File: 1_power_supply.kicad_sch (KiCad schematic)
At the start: 38 parts

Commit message: feat: power supply updates and mcu kickoff
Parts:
- added C?: 100u, symbol Device:C_Polarized_Small
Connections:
- net +BATT: now also C?.1
- net GND: now also C?.2
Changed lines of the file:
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@@
   (junction (at 190.5 64.77) (diameter 0) (color 0 0 0 0)
   )
+  (junction (at 238.125 61.595) (diameter 0) (color 0 0 0 0)
+  )
   (junction (at 217.805 61.595) (diameter 0) (color 0 0 0 0)
   )
@@
   (junction (at 29.845 66.04) (diameter 0) (color 0 0 0 0)
   )
+  (junction (at 238.125 50.165) (diameter 0) (color 0 0 0 0)
+  )
   (junction (at 39.37 111.76) (diameter 0) (color 0 0 0 0)
   )
@@
     (stroke (width 0) (type default) (color 0 0 0 0))
   )
-  (polyline (pts (xy 249.555 36.83) (xy 209.55 36.83))
+  (polyline (pts (xy 259.715 36.83) (xy 209.55 36.83))
     (stroke (width 0) (type default) (color 0 0 0 0))
   )
@@
     (stroke (width 0) (type default) (color 0 0 0 0))
   )
-  (polyline (pts (xy 209.55 80.01) (xy 249.555 80.01))
+  (polyline (pts (xy 209.55 80.01) (xy 259.715 80.01))
     (stroke (width 0) (type default) (color 0 0 0 0))
   )
@@
     (stroke (width 0) (type default) (color 0 0 0 0))
   )
+  (wire (pts (xy 248.285 53.34) (xy 248.285 50.165))
+    (stroke (width 0) (type default) (color 0 0 0 0))
+  )
   (wire (pts (xy 91.44 111.76) (xy 93.98 111.76))
     (stroke (width 0) (type default) (color 0 0 0 0))
@@
     (stroke (width 0) (type default) (color 0 0 0 0))
   )
+  (wire (pts (xy 248.285 61.595) (xy 238.125 61.595))
+    (stroke (width 0) (type default) (color 0 0 0 0))
+  )
   (wire (pts (xy 66.04 53.975) (xy 66.04 62.23))
     (stroke (width 0) (type default) (color 0 0 0 0))
@@
     (stroke (width 0) (type default) (color 0 0 0 0))
   )
-  (polyline (pts (xy 249.555 80.01) (xy 249.555 36.83))
+  (polyline (pts (xy 259.715 80.01) (xy 259.715 36.83))
     (stroke (width 0) (type default) (color 0 0 0 0))
   )
@@
     (stroke (width 0) (type default) (color 0 0 0 0))
   )
+  (wire (pts (xy 248.285 58.42) (xy 248.285 61.595))
+    (stroke (width 0) (type default) (color 0 0 0 0))
+  )
   (wire (pts (xy 81.915 78.105) (xy 81.915 80.01))
     (stroke (width 0) (type default) (color 0 0 0 0))
@@
   )
   (wire (pts (xy 101.6 111.76) (xy 106.045 111.76))
+    (stroke (width 0) (type default) (color 0 0 0 0))
+  )
+  (wire (pts (xy 248.285 50.165) (xy 238.125 50.165))
     (stroke (width 0) (type default) (color 0 0 0 0))
   )
@@
       (effects (font (size 1.27 1.27)) hide)
     )
+    (pin "1")
+    (pin "2")
+  )
+  (symbol (lib_id "Device:C_Polarized_Small") (at 248.285 55.88 0) (unit 1)
+    (in_bom yes) (on_board yes)
+    (property "Reference" "C?" (id 0) (at 250.825 54.61 0)
+      (effects (font (size 1.27 1.27)) (justify left))
+    )
+    (property "Value" "100u" (id 1) (at 250.825 57.15 0)
+      (effects (font (size 1.27 1.27)) (justify left))
+    )
+    (property "Footprint" "" (id 2) (at 248.285 55.88 0)
+      (effects (font (size 1.27 1.27)) hide)
+    )
+    (property "Datasheet" "~" (id 3) (at 248.285 55.88 0)
+      (effects (font (size 1.27 1.27)) hide)
+    )

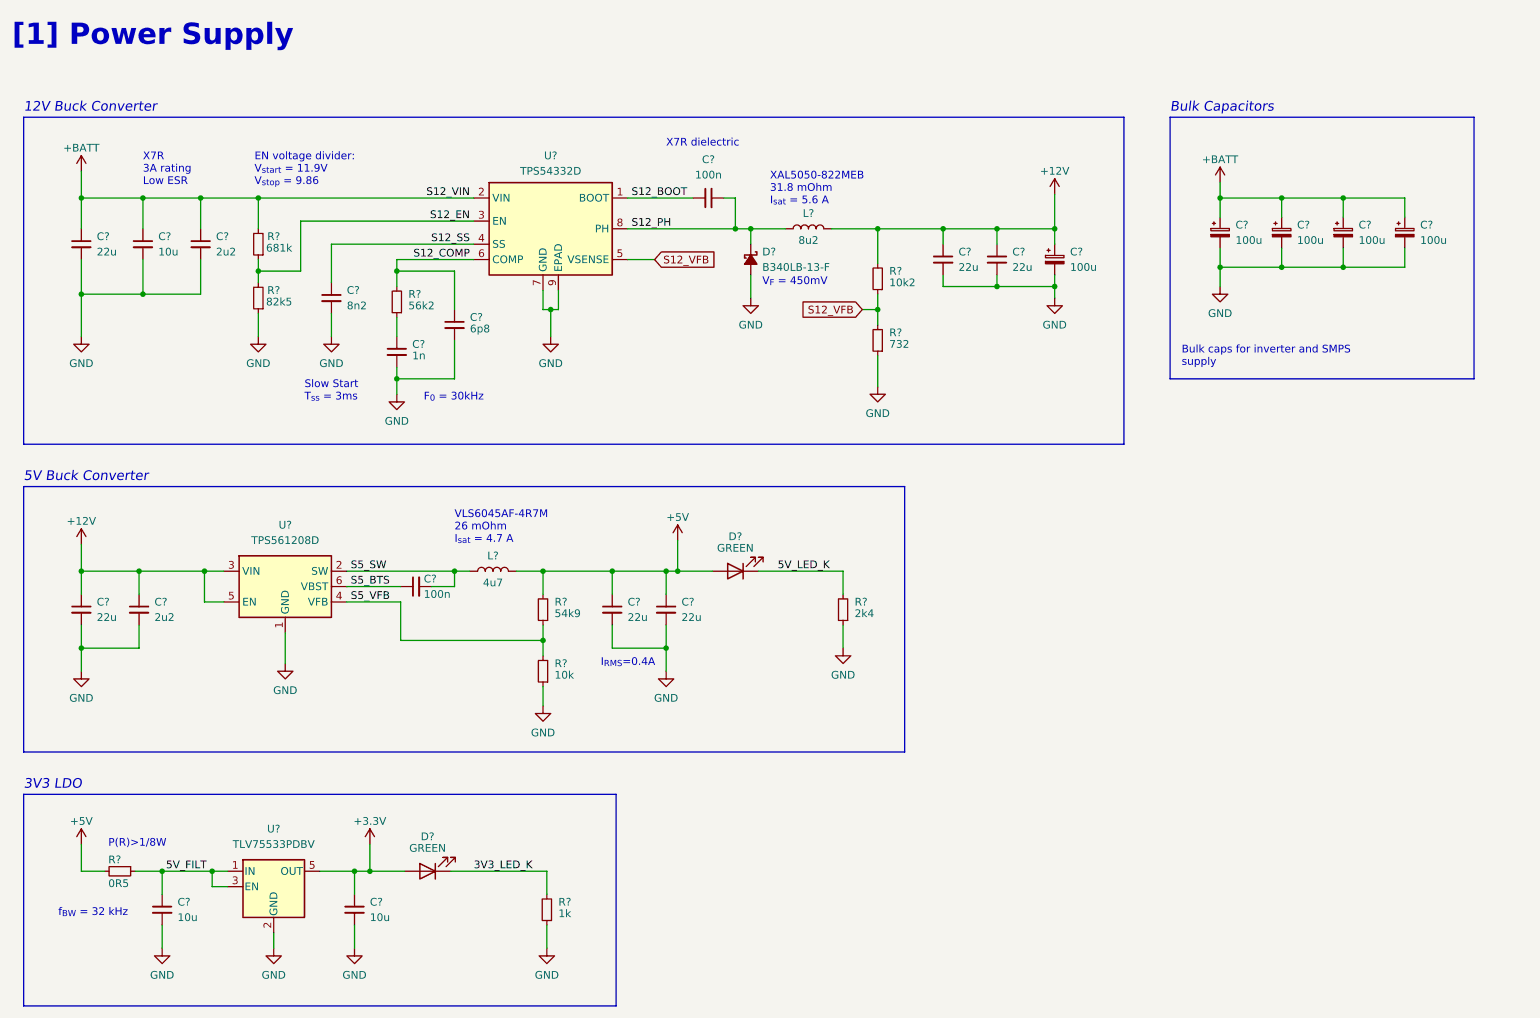
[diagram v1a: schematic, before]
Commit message: feat/chore: MCU supply caps and filter circuitry and updated component references in power supply sheet
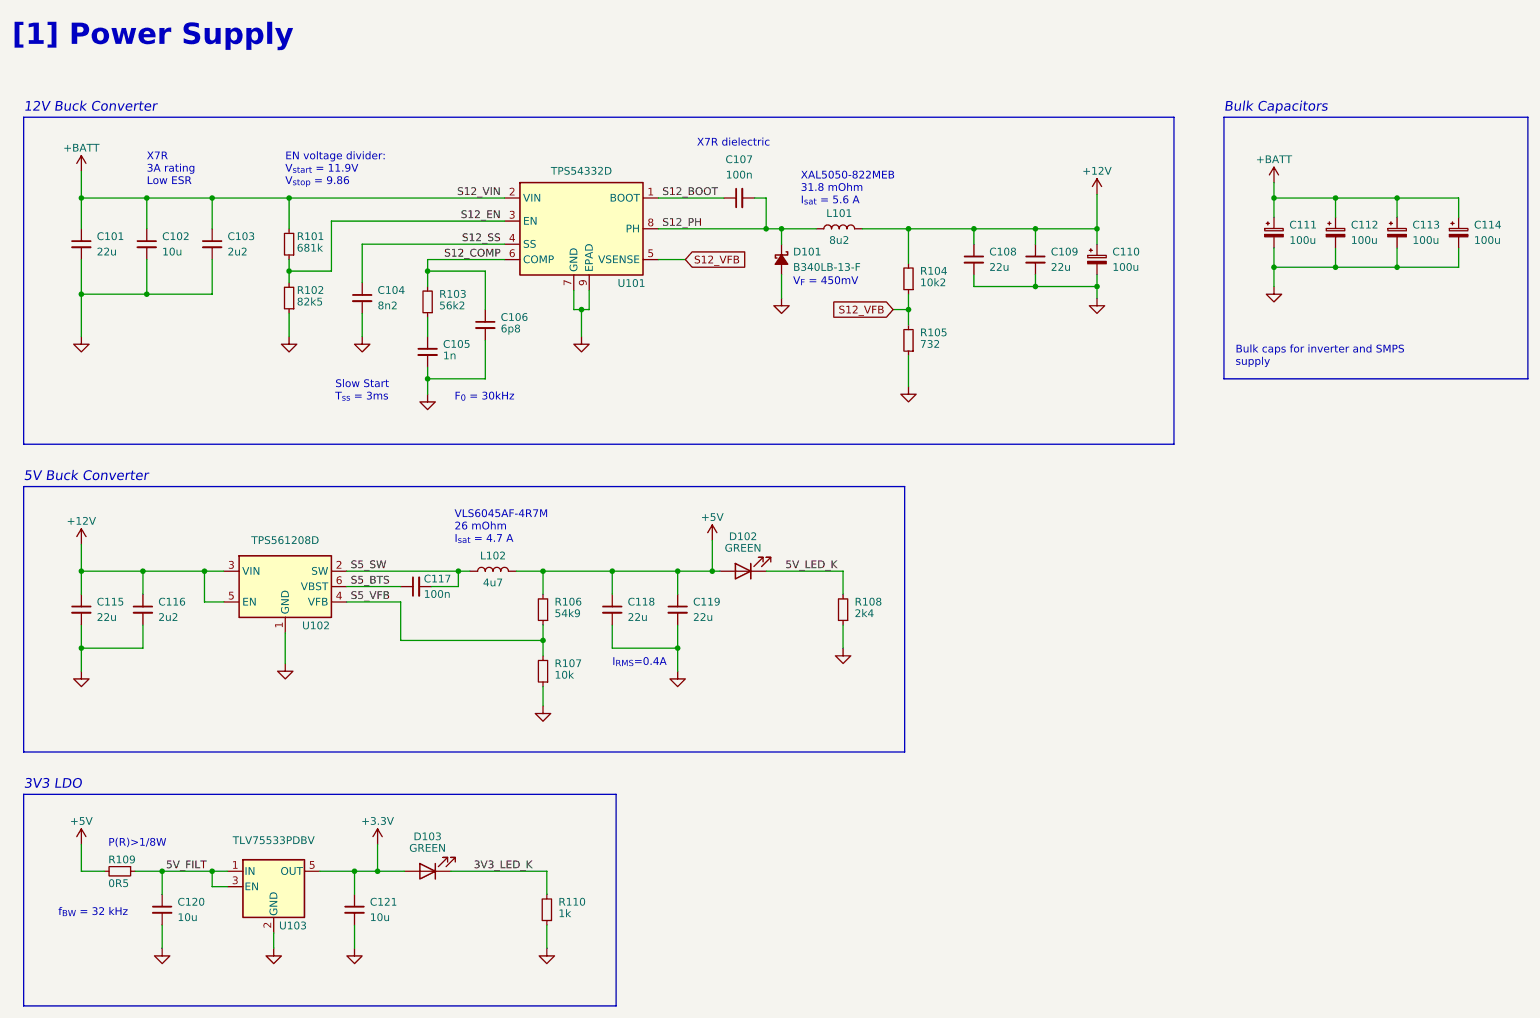
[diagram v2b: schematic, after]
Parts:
- gave numbers to parts that had none: 39
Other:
- moved on the sheet: C102, C103, C104, C105, C106, C107, C108, C109, C110, C111, C112, C113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

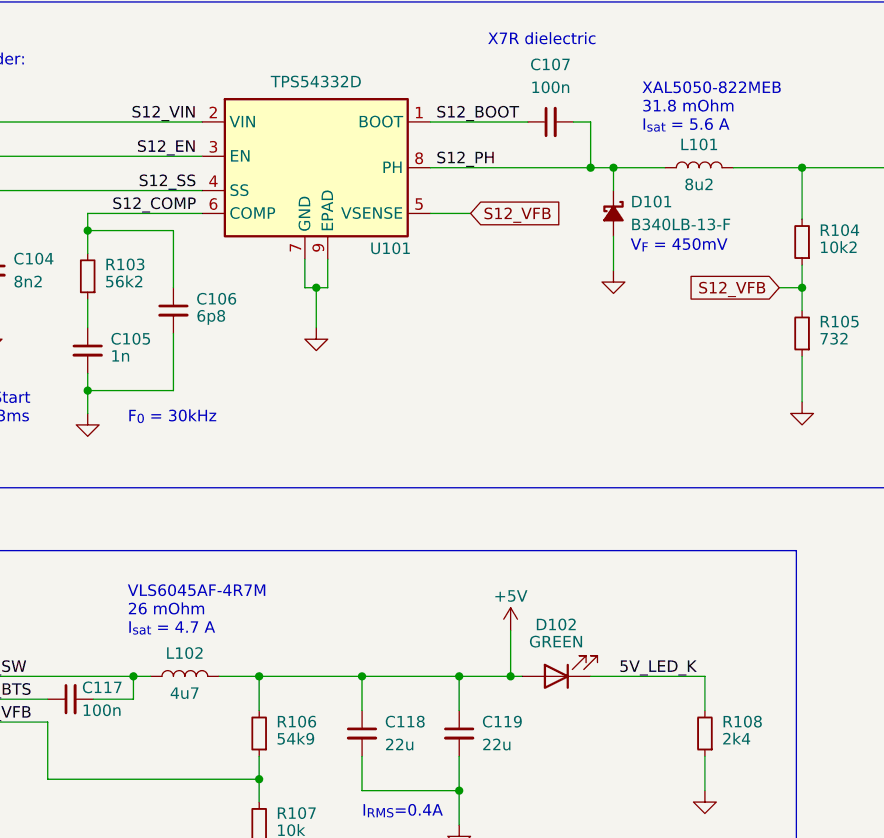
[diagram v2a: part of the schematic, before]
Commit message: feat: initial peripheral circuitry for MCU
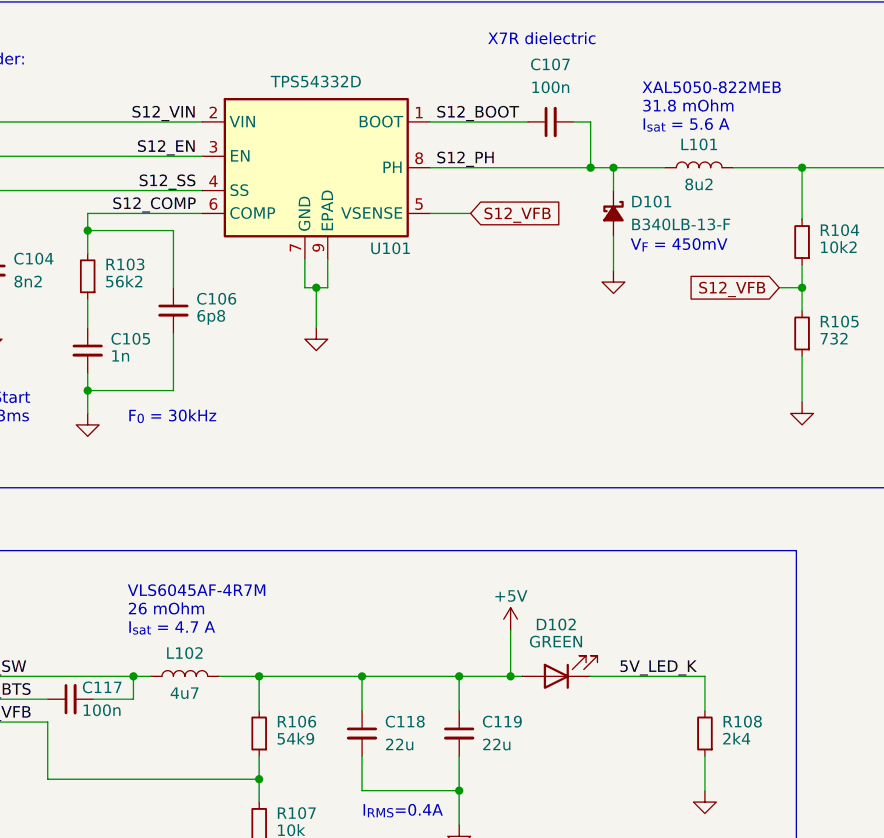
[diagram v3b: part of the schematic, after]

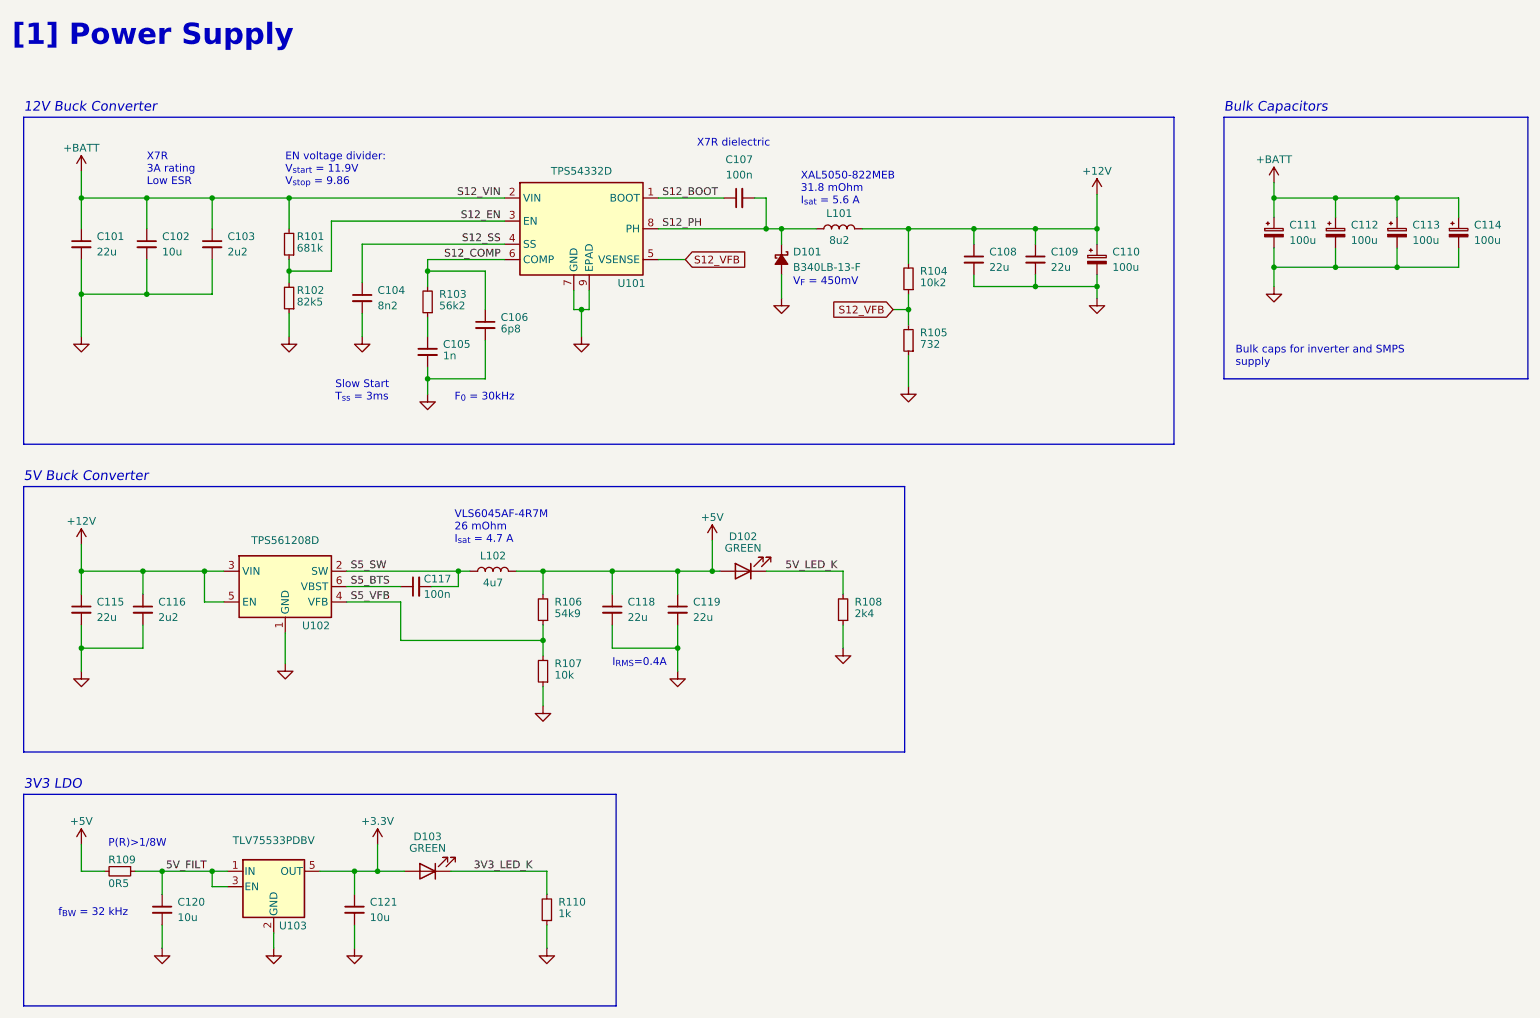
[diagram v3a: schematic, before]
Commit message: feat: 5V power supply selection
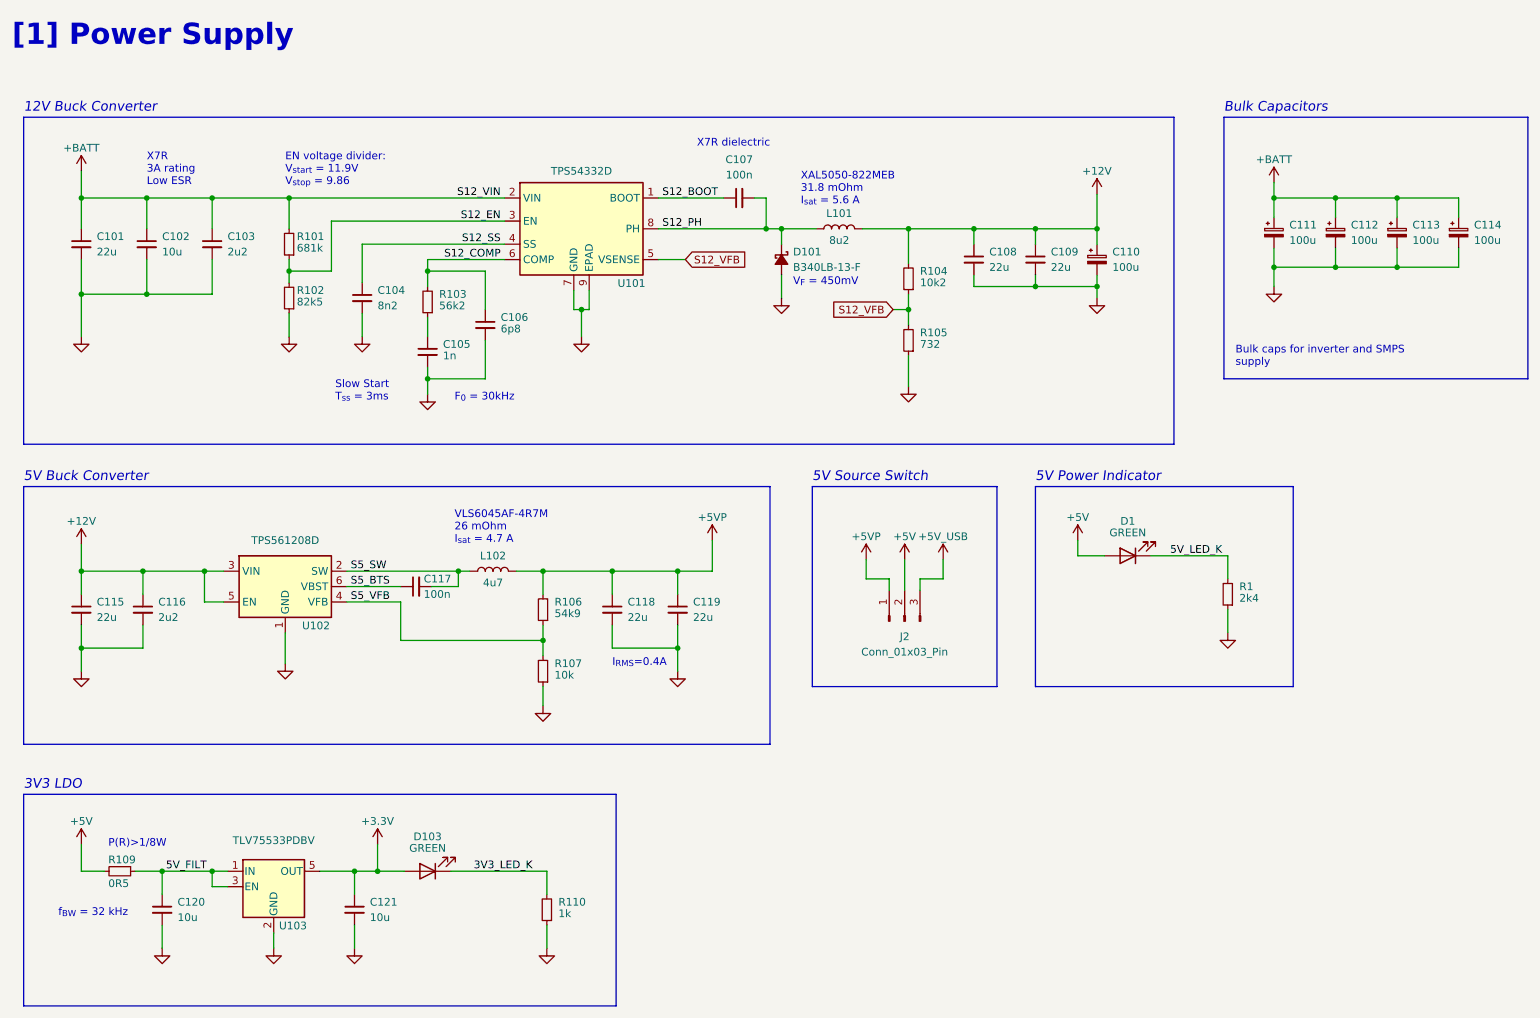
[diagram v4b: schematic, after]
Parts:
- removed D102: GREEN, symbol Device:LED
- removed R108: 2k4, symbol Device:R_Small
- added D1: GREEN, symbol Device:LED
- added J2: Conn_01x03_Pin, symbol Connector:Conn_01x03_Pin
- added R1: 2k4, symbol Device:R_Small
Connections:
- net +5V: now also D1.2 (A), J2.2 (Pin_2), J2.3 (Pin_3); no longer C118.1, C119.1, L102.2, R106.2
- net 5V_LED_K: now also D1.1 (K), R1.2
- net GND: now also R1.1
- new net +5VP: C118.1, C119.1, J2.1 (Pin_1), L102.2, R106.2
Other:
- note added: "5V Power Indicator"
- note added: "5V Source Switch"

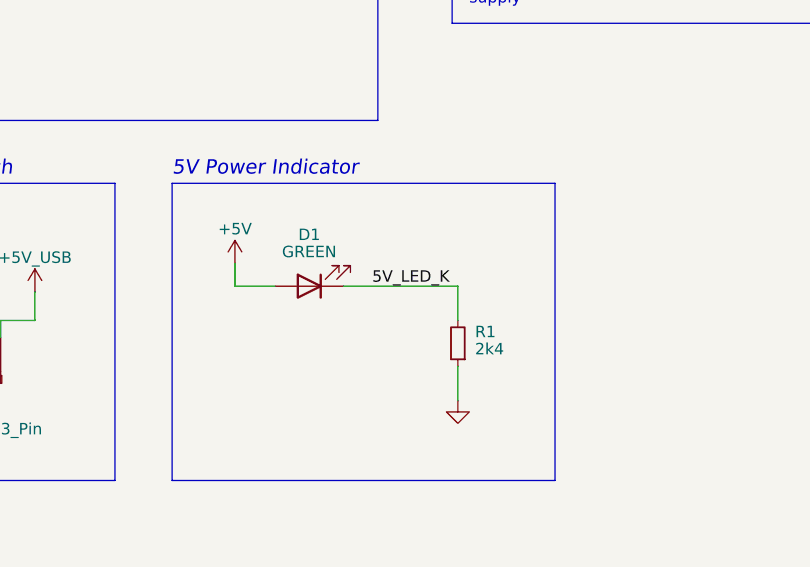
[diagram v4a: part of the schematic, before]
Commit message: feat: new phases, LED pins
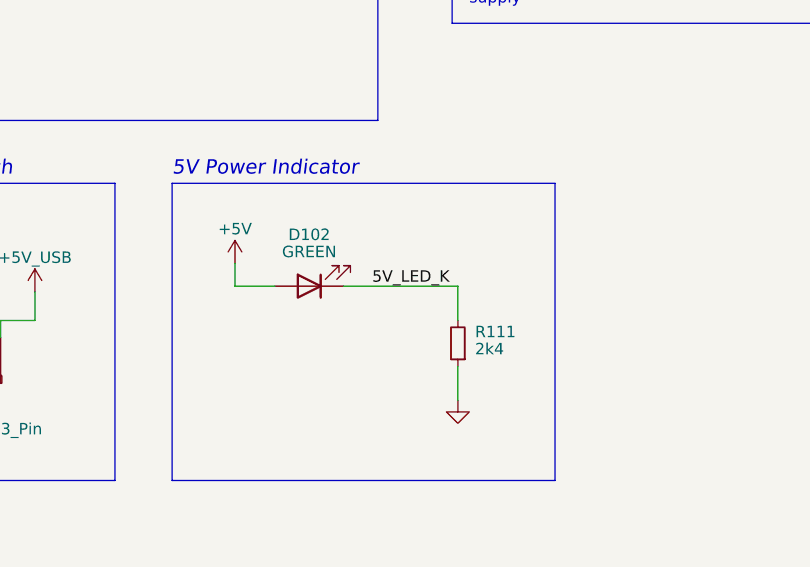
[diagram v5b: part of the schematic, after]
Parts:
- renumbered D1 to D102, R1 to R111
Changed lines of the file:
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@@
   (symbol (lib_id "Device:LED") (at 202.565 109.22 180) (unit 1)
     (in_bom yes) (on_board yes) (dnp no)
-    (property "Reference" "D1" (at 202.565 103.505 0)
+    (property "Reference" "D102" (at 202.565 103.505 0)
       (effects (font (size 1.27 1.27)))
     )
@@
       (project "ESC_R1"
         (path "/9dea2e18-5867-4ed4-a12d-7ee109225de0/bab0431c-ca33-4c57-9dbe-00ccaf05ca0f"
-          (reference "D1") (unit 1)
+          (reference "D102") (unit 1)
         )
       )
@@
   (symbol (lib_id "Device:R_Small") (at 219.075 115.57 180) (unit 1)
     (in_bom yes) (on_board yes) (dnp no)
-    (property "Reference" "R1" (at 220.98 114.3 0)
+    (property "Reference" "R111" (at 220.98 114.3 0)
       (effects (font (size 1.27 1.27)) (justify right))
     )
@@
       (project "ESC_R1"
         (path "/9dea2e18-5867-4ed4-a12d-7ee109225de0/bab0431c-ca33-4c57-9dbe-00ccaf05ca0f"
-          (reference "R1") (unit 1)
-        )
-      )
+          (reference "R111") (unit 1)
+        )
+      )
